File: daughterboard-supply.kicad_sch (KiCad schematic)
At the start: 17 parts

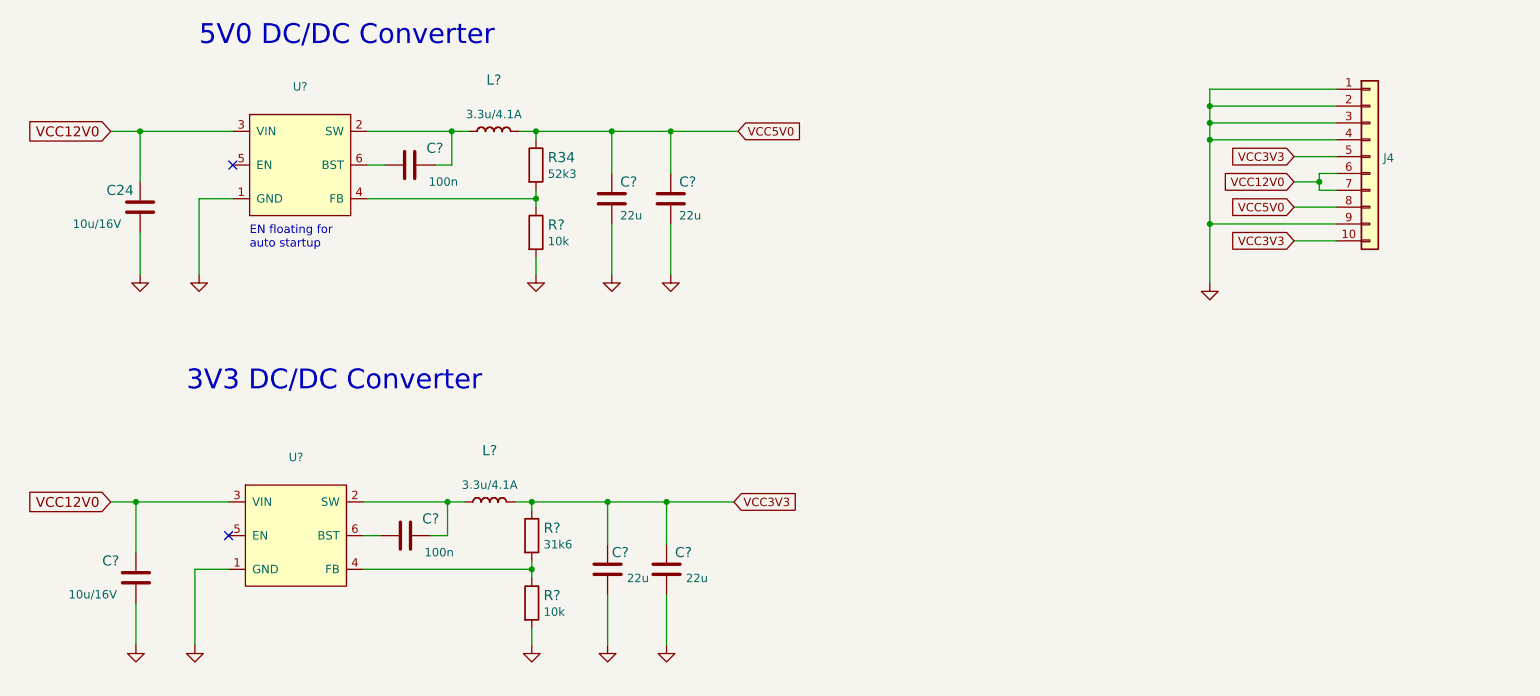
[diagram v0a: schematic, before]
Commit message: Fixed FTDI sheet
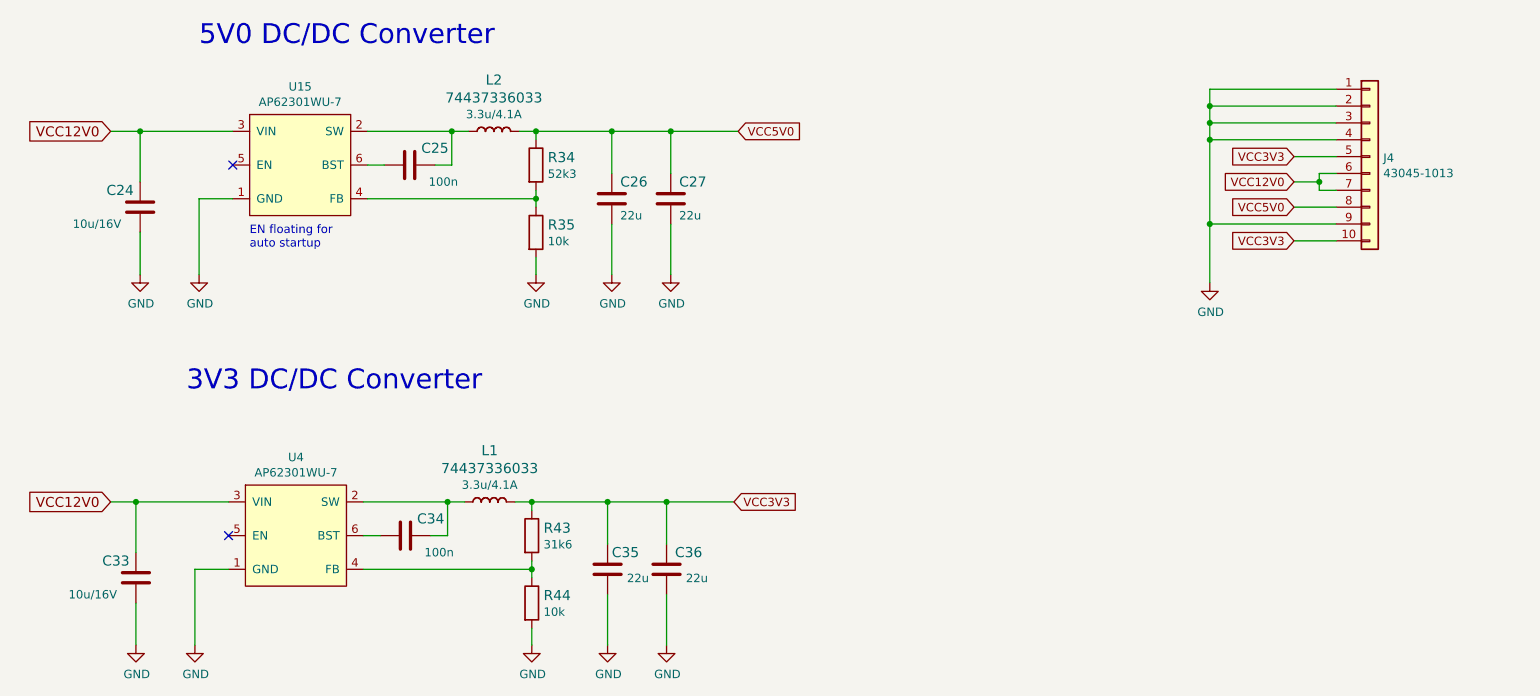
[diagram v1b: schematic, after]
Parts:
- C24: value (none) -> C_10u_16V_0603; footprint (none) -> nuc-compute-cluster-power-breakout-footprints:0603-cap
- C25, C34: renamed from C?; value (none) -> C_100n_0402; footprint (none) -> nuc-compute-cluster-power-breakout-footprints:0402-cap
- C26, C27, C35, C36: renamed from C?; value (none) -> C_22u_0603; footprint (none) -> nuc-compute-cluster-power-breakout-footprints:0603-cap
- C33: renamed from C?; value (none) -> C_10u_16V_0603; footprint (none) -> nuc-compute-cluster-power-breakout-footprints:0603-cap
- J4: value (none) -> 43045-1013; footprint (none) -> nuc-compute-cluster-power-breakout-footprints:43045-1013
- L1, L2: renamed from L?; value (none) -> 74437336033; footprint (none) -> nuc-compute-cluster-power-breakout-footprints:WE_74437336033
- R34: value (none) -> R_52k3_0402; footprint (none) -> nuc-compute-cluster-power-breakout-footprints:0402-res
- R35, R44: renamed from R?; value (none) -> R_10k_0402; footprint (none) -> nuc-compute-cluster-power-breakout-footprints:0402-res
- R43: renamed from R?; value (none) -> R_31k6_0402; footprint (none) -> nuc-compute-cluster-power-breakout-footprints:0402-res
- U15, U4: renamed from U?; value (none) -> AP62301WU-7; footprint (none) -> nuc-compute-cluster-power-breakout-footprints:TSOT23-6

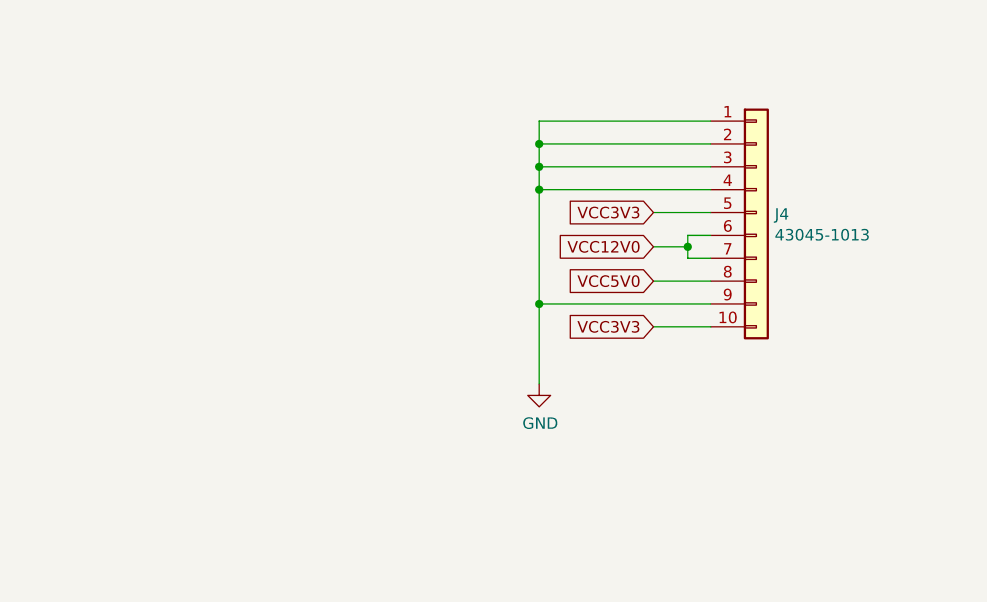
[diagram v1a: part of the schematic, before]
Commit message: Changed power connectors
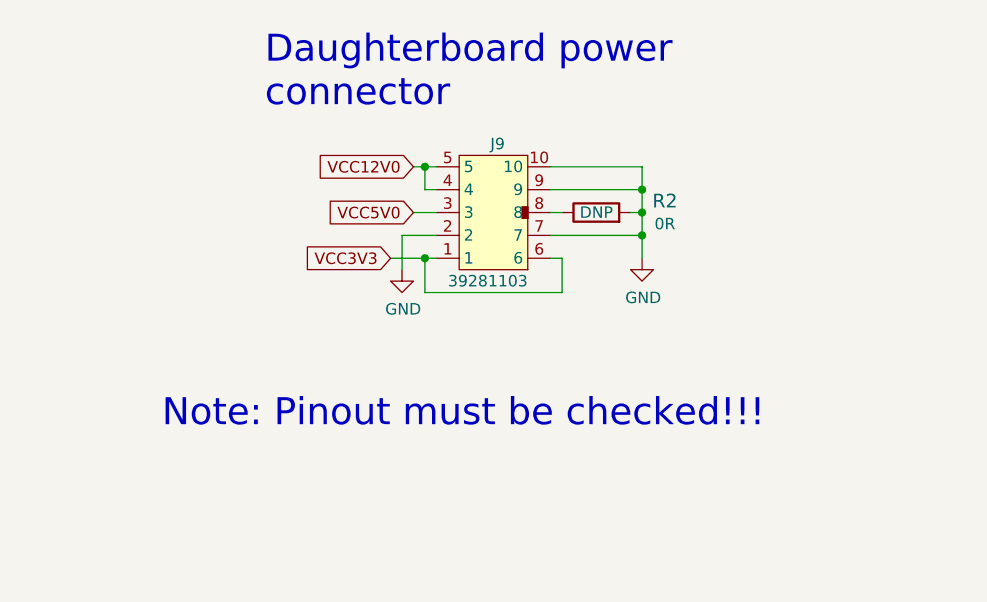
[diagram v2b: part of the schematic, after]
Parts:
- removed J4: 43045-1013, nuc-compute-cluster-power-breakout-footprints:43045-1013, symbol nuc-compute-cluster-power-breakout:43045-1013
- added J9: 39281103, antmicro-footprints:MOLEX_39281103, symbol antmicroRectangularConnectorsHeadersMalePins:39281103
- added R2: R_0R_0402, antmicro-footprints:0402-res, symbol antmicroResistors0402:R_0R_0402
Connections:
- net GND: now also J9.10, J9.2, J9.7, J9.9, R2.2
- net VCC12V0: now also J9.4, J9.5
- net VCC3V3: now also J9.1, J9.6
- net VCC5V0: now also J9.3
- new net: J9.8, R2.1
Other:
- note added: "Daughterboard power connector"
- note added: "Note: Pinout must be checked!!!"

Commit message: Revision bump to 1.3.0
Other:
- title: (none) -> NUC Computer Cluster Power Breakout HW
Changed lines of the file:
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@@
 (kicad_sch (version 20211123) (generator eeschema)
   (paper "A4")
+  (title_block
+    (title "NUC Computer Cluster Power Breakout HW")
+    (date "2022-07-29")
+    (rev "1.3.0")
+  )
   (junction (at 232.41 49.53) (diameter 0) (color 0 0 0 0)
   )

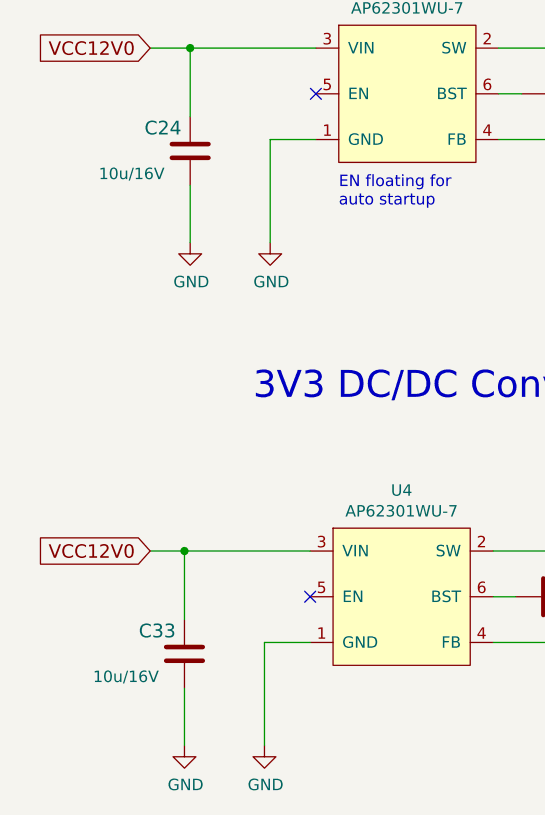
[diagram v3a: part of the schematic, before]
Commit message: Added support for default off and changed converter cap voltage rating
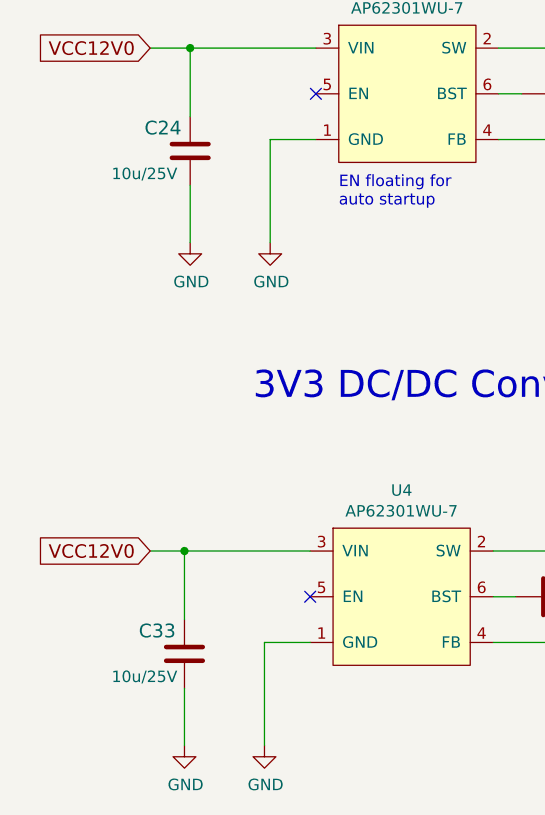
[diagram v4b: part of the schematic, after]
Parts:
- C24, C33: symbol nuc-compute-cluster-power-breakout:C_10u_16V_0603 -> nuc-compute-cluster-power-breakout:C_10u_25V_0603; MPN GRM188C81C106MA73D -> C1608X5R1E106M080AC; Manufacturer MURATA -> TDK; Val 10u/16V -> 10u/25V
- J9: footprint antmicro-footprints:MOLEX_39281103 -> nuc-compute-cluster-power-breakout-footprints:MOLEX_39281103; symbol antmicroRectangularConnectorsHeadersMalePins:39281103 -> nuc-compute-cluster-power-breakout:39281103
- R2: footprint antmicro-footprints:0402-res -> nuc-compute-cluster-power-breakout-footprints:0402-res; symbol antmicroResistors0402:R_0R_0402 -> nuc-compute-cluster-power-breakout:R_0R_0402
